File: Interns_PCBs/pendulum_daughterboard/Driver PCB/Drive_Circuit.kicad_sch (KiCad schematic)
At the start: 17 parts, among them IC5 MAX9928FAUA+, J2 Coil, Q1 BC557, Q2 BC547

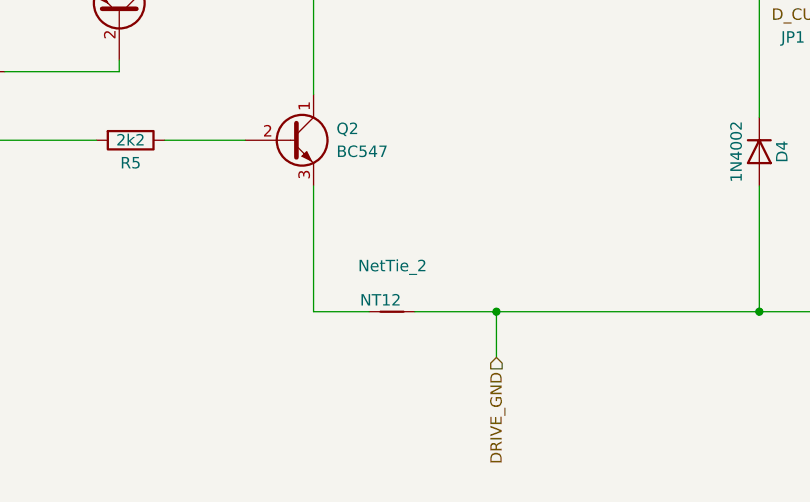
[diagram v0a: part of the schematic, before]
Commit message: Changed Diode
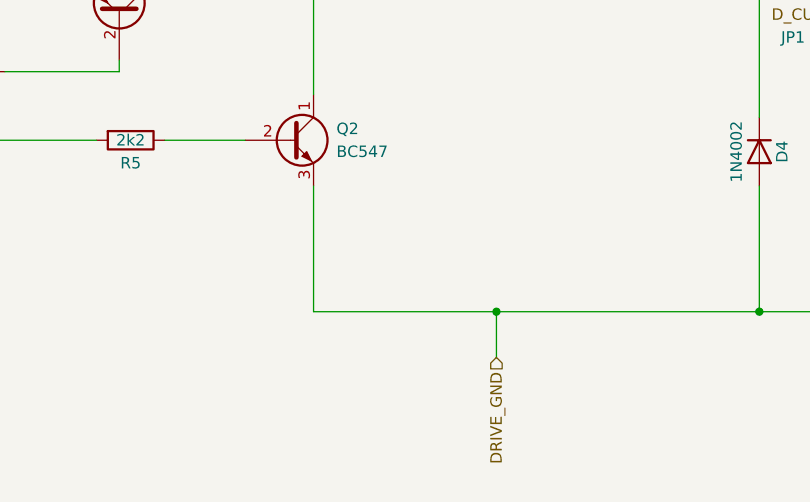
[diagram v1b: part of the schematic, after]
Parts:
- removed NT12: NetTie_2, NetTie:NetTie-2_SMD_Pad0.5mm, symbol Device:NetTie_2
- D4: footprint Diode_SMD:D_0603_1608Metric_Pad1.05x0.95mm_HandSolder -> Diode_THT:D_T-1_P5.08mm_Horizontal
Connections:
- net DRIVE_GND: now also Q2.3 (E)
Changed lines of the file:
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@@
     (stroke (width 0) (type default) (color 0 0 0 0))
   )
-  (wire (pts (xy 119.2062 110.49) (xy 113.03 110.49))
+  (wire (pts (xy 113.03 110.49) (xy 133.35 110.49))
     (stroke (width 0) (type default) (color 0 0 0 0))
   )
@@
     (stroke (width 0) (type default) (color 0 0 0 0))
   )
-  (wire (pts (xy 133.35 110.49) (xy 124.2862 110.49))
-    (stroke (width 0) (type default) (color 0 0 0 0))
-  )
   (hierarchical_label "D_GND" (shape input) (at 269.24 77.47 0)
     (effects (font (size 1.27 1.27)) (justify left))
@@
   (hierarchical_label "DRIVE_GND" (shape input) (at 133.35 115.57 270)
     (effects (font (size 1.27 1.27)) (justify right))
-  )
-  (symbol (lib_id "Device:NetTie_2") (at 121.7462 110.49 0) (unit 1)
-    (in_bom yes) (on_board yes)
-    (property "Reference" "NT12" (id 0) (at 120.4762 109.22 0))
-    (property "Value" "NetTie_2" (id 1) (at 121.8031 105.41 0))
-    (property "Footprint" "NetTie:NetTie-2_SMD_Pad0.5mm" (id 2) (at 121.7462 110.49 0)
-      (effects (font (size 1.27 1.27)) hide)
-    )
-    (property "Datasheet" "~" (id 3) (at 121.7462 110.49 0)
-      (effects (font (size 1.27 1.27)) hide)
-    )
-    (pin "1")
-    (pin "2")
   )
   (symbol (lib_id "Device:R") (at 92.71 91.44 270) (unit 1)
@@
     (property "Reference" "D4" (id 0) (at 165.1 92.71 0))
     (property "Value" "1N4002" (id 1) (at 160.02 92.71 0))
-    (property "Footprint" "Diode_SMD:D_0603_1608Metric_Pad1.05x0.95mm_HandSolder" (id 2) (at 162.56 92.71 0)
+    (property "Footprint" "Diode_THT:D_T-1_P5.08mm_Horizontal" (id 2) (at 162.56 92.71 0)
       (effects (font (size 1.27 1.27)) hide)
     )

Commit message: Friday Updates
24/06/22
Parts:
- J2: footprint TerminalBlock_TE-Connectivity:TerminalBlock_TE_282834-2_1x02_P2.54mm_Horizontal -> Connector_Molex:RSPROPenduinoTerminal
- Q1, Q2: footprint Package_TO_SOT_SMD:SOT-523 -> Package_TO_SOT_SMD:SOT-23
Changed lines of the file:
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@@
     (property "Reference" "J2" (id 0) (at 188.595 92.71 0))
     (property "Value" "Coil" (id 1) (at 188.595 95.25 0))
-    (property "Footprint" "TerminalBlock_TE-Connectivity:TerminalBlock_TE_282834-2_1x02_P2.54mm_Horizontal" (id 2) (at 189.23 100.33 0)
+    (property "Footprint" "Connector_Molex:RSPROPenduinoTerminal" (id 2) (at 189.23 100.33 0)
       (effects (font (size 1.27 1.27)) hide)
     )
@@
     (property "Reference" "Q1" (id 0) (at 91.44 68.58 90))
     (property "Value" "BC557" (id 1) (at 91.44 71.12 90))
-    (property "Footprint" "Package_TO_SOT_SMD:SOT-523" (id 2) (at 89.535 72.39 0)
+    (property "Footprint" "Package_TO_SOT_SMD:SOT-23" (id 2) (at 89.535 72.39 0)
       (effects (font (size 1.27 1.27) italic) (justify left) hide)
     )
@@
       (effects (font (size 1.27 1.27)) (justify left))
     )
-    (property "Footprint" "Package_TO_SOT_SMD:SOT-523" (id 2) (at 115.57 93.345 0)
+    (property "Footprint" "Package_TO_SOT_SMD:SOT-23" (id 2) (at 115.57 93.345 0)
       (effects (font (size 1.27 1.27) italic) (justify left) hide)
     )
